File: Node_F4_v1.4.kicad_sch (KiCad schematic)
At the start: 87 parts, among them J1 Screw_Terminal_01x02, J3 Screw_Terminal_01x02, J4 Screw_Terminal_01x02, J5 Screw_Terminal_01x03, J6 Conn_01x16_Female, J7 Conn_01x08_Male, J8 STLINK, Q1 P_Mosfet, SW1 SW_Push, U10 Ai-Thinker-Ra-02, U2 PCF8574A, U3 AMS1117-3.3, U4 DS3231M, U5 MAX485E, U6 STM32F411CEUx, U7 Trans_MOSFET, U8 Trans_MOSFET, U9 W25Q128JVS, Y1 25MHz

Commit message: sua nguon
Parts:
- R19: footprint Resistor_SMD:R_0603_1608Metric -> Resistor_SMD:R_0805_2012Metric
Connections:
- net L: now also J3.2 (Pin_2), J4.2 (Pin_2)
- net N: now also RL1.2, RL2.2; no longer J3.1 (Pin_1), J4.1 (Pin_1), RL1.3, RL2.3
- removed net relay_1: J4.2 (Pin_2), RL1.2
- removed net relay_2: J3.2 (Pin_2), RL2.2
- new net N1: J4.1 (Pin_1), RL1.3
- new net N2: J3.1 (Pin_1), RL2.3
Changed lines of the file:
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@@
     (stroke (width 0) (type default) (color 0 0 0 0))
   )
-  (wire (pts (xy 360.68 38.1) (xy 365.76 38.1))
+  (wire (pts (xy 360.68 38.1) (xy 370.84 38.1))
     (stroke (width 0) (type default) (color 0 0 0 0))
   )
@@
     (effects (font (size 1.27 1.27)) (justify left bottom))
   )
-  (label "N" (at 62.23 189.23 0)
+  (label "N2" (at 62.23 189.23 0)
     (effects (font (size 1.27 1.27)) (justify left bottom))
   )
@@
     (effects (font (size 1.27 1.27)) (justify right bottom))
   )
+  (label "N" (at 367.03 68.58 180)
+    (effects (font (size 1.27 1.27)) (justify right bottom))
+  )
   (label "TFT_RS" (at 64.77 224.79 0)
     (effects (font (size 1.27 1.27)) (justify left bottom))
@@
     (effects (font (size 1.27 1.27)) (justify right bottom))
   )
-  (label "relay_2" (at 62.23 191.77 0)
-    (effects (font (size 1.27 1.27)) (justify left bottom))
-  )
   (label "TFT_CS" (at 240.03 189.23 0)
     (effects (font (size 1.27 1.27)) (justify left bottom))
@@
     (effects (font (size 1.27 1.27)) (justify left bottom))
   )
+  (label "N" (at 368.3 22.86 0)
+    (effects (font (size 1.27 1.27)) (justify left bottom))
+  )
   (label "TFT_DB7" (at 240.03 201.93 0)
     (effects (font (size 1.27 1.27)) (justify left bottom))
@@
     (effects (font (size 1.27 1.27)) (justify left bottom))
   )
-  (label "relay_1" (at 367.03 68.58 180)
-    (effects (font (size 1.27 1.27)) (justify right bottom))
-  )
-  (label "N" (at 62.23 195.58 0)
+  (label "N1" (at 62.23 195.58 0)
     (effects (font (size 1.27 1.27)) (justify left bottom))
   )
@@
     (effects (font (size 1.27 1.27)) (justify left bottom))
   )
-  (label "relay_2" (at 368.3 22.86 180)
-    (effects (font (size 1.27 1.27)) (justify right bottom))
+  (label "L" (at 62.23 198.12 0)
+    (effects (font (size 1.27 1.27)) (justify left bottom))
   )
   (label "TFT_DB2" (at 64.77 242.57 0)
@@
     (effects (font (size 1.27 1.27)) (justify left bottom))
   )
-  (label "N" (at 367.03 83.82 180)
+  (label "N1" (at 367.03 83.82 180)
     (effects (font (size 1.27 1.27)) (justify right bottom))
   )
@@
     (effects (font (size 1.27 1.27)) (justify left bottom))
   )
+  (label "L" (at 62.23 191.77 0)
+    (effects (font (size 1.27 1.27)) (justify left bottom))
+  )
   (label "P6" (at 107.95 199.39 0)
     (effects (font (size 1.27 1.27)) (justify left bottom))
@@
     (effects (font (size 1.27 1.27)) (justify right bottom))
   )
-  (label "relay_1" (at 62.23 198.12 0)
-    (effects (font (size 1.27 1.27)) (justify left bottom))
-  )
   (label "SPI_SCK" (at 340.36 201.93 0)
     (effects (font (size 1.27 1.27)) (justify left bottom))
@@
     (effects (font (size 1.27 1.27)) (justify left bottom))
   )
-  (label "N" (at 365.76 38.1 180)
+  (label "N2" (at 370.84 38.1 180)
     (effects (font (size 1.27 1.27)) (justify right bottom))
   )
@@
     (property "Reference" "R19" (id 0) (at 58.42 228.6 90))
     (property "Value" "100R" (id 1) (at 58.42 231.14 90))
-    (property "Footprint" "Resistor_SMD:R_0603_1608Metric" (id 2) (at 58.42 236.728 90)
+    (property "Footprint" "Resistor_SMD:R_0805_2012Metric" (id 2) (at 58.42 236.728 90)
       (effects (font (size 1.27 1.27)) hide)
     )
@@
     )
     (path "/80ad6425-d2d2-43d9-b7b6-efb83d17a2ad"
-      (reference "R19") (unit 1) (value "100R") (footprint "Resistor_SMD:R_0603_1608Metric")
+      (reference "R19") (unit 1) (value "100R") (footprint "Resistor_SMD:R_0805_2012Metric")
     )
     (path "/d640f459-d51e-4801-88fe-79ada9526d0a"

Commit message: thay terminal
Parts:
- removed J1, J3, J4: Screw_Terminal_01x02, TerminalBlock_Phoenix:TerminalBlock_Phoenix_MKDS-1,5-2-5.08_1x02_P5.08mm_Horizontal, symbol Connector:Screw_Terminal_01x02
- removed J5: Screw_Terminal_01x03, TerminalBlock_Phoenix:TerminalBlock_Phoenix_MKDS-1,5-3-5.08_1x03_P5.08mm_Horizontal, symbol Connector:Screw_Terminal_01x03
- added J?: Screw_Terminal_01x09, TerminalBlock_Phoenix:TerminalBlock_Phoenix_MKDS-1,5-9_1x09_P5.00mm_Horizontal, symbol Connector:Screw_Terminal_01x09
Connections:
- net A+: now also J?.7 (Pin_7)
- net B-: now also J?.9 (Pin_9)
- net GNDREF: now also J?.8 (Pin_8)
- net L: now also J?.1 (Pin_1), J?.4 (Pin_4), J?.6 (Pin_6)
- net N: now also J?.2 (Pin_2)
- net N1: now also J?.5 (Pin_5)
- net N2: now also J?.3 (Pin_3)

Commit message: teardrop
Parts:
- gave numbers to parts that had none: 1
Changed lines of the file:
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@@
   (symbol (lib_id "Connector:Screw_Terminal_01x09") (at 54.61 194.31 0) (unit 1)
     (in_bom yes) (on_board yes) (fields_autoplaced)
-    (property "Reference" "J?" (id 0) (at 57.15 193.0399 0)
+    (property "Reference" "J1" (id 0) (at 57.15 193.0399 0)
       (effects (font (size 1.27 1.27)) (justify left))
     )
@@
   (symbol (lib_id "power:GNDREF") (at 31.75 201.93 180) (unit 1)
     (in_bom yes) (on_board yes)
-    (property "Reference" "#PWR?" (id 0) (at 31.75 195.58 0)
+    (property "Reference" "#PWR0102" (id 0) (at 31.75 195.58 0)
       (effects (font (size 1.27 1.27)) hide)
     )
@@
       (reference "#PWR0101") (unit 1) (value "+5V") (footprint "")
     )
+    (path "/af3ac857-dd8e-4784-92ee-7d191ec5a304"
+      (reference "#PWR0102") (unit 1) (value "GNDREF") (footprint "")
+    )
     (path "/f840a601-70b7-488e-8299-6289e9e09ecc"
       (reference "#PWR0103") (unit 1) (value "+3.3V") (footprint "")
@@
       (reference "#PWR0158") (unit 1) (value "GND") (footprint "")
     )
-    (path "/af3ac857-dd8e-4784-92ee-7d191ec5a304"
-      (reference "#PWR?") (unit 1) (value "GNDREF") (footprint "")
-    )
     (path "/e79c523e-5bda-47a2-9098-db791a1676cd"
       (reference "BT1") (unit 1) (value "Battery_Cell") (footprint "IVS_FOOTPRINTS:BatteryHolder_CR1220")
@@
       (reference "H4") (unit 1) (value "MountingHole") (footprint "MountingHole:MountingHole_2.2mm_M2_Pad_Via")
     )
+    (path "/a20ced64-33cc-4c5f-9ebb-67e3de71ad6f"
+      (reference "J1") (unit 1) (value "Screw_Terminal_01x09") (footprint "TerminalBlock_Phoenix:TerminalBlock_Phoenix_MKDS-1,5-9_1x09_P5.00mm_Horizontal")
+    )
     (path "/5825f3f3-cb85-465a-8d89-39ae74babb06"
       (reference "J6") (unit 1) (value "Conn_01x16_Female") (footprint "Connector_PinSocket_2.54mm:PinSocket_1x16_P2.54mm_Vertical")
@@
       (reference "J8") (unit 1) (value "STLINK") (footprint "Connector_PinHeader_2.54mm:PinHeader_1x05_P2.54mm_Vertical")
     )
-    (path "/a20ced64-33cc-4c5f-9ebb-67e3de71ad6f"
-      (reference "J?") (unit 1) (value "Screw_Terminal_01x09") (footprint "TerminalBlock_Phoenix:TerminalBlock_Phoenix_MKDS-1,5-9_1x09_P5.00mm_Horizontal")
-    )
     (path "/c09e0fa3-9a7c-4b7a-ba41-09c83225f659"

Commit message: DONE
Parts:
- removed R18: 1K, Resistor_SMD:R_0603_1608Metric, symbol Device:R
- added BZ1: Buzzer, Buzzer_Beeper:PUIAudio_SMT_0825_S_4_R, symbol Device:Buzzer
- added Q2: MMBT3904L, IVS_FOOTPRINTS:SOT23-3, symbol IVS_Symbol:MMBT3904L
- R19: value 100R -> 1K; footprint Resistor_SMD:R_0805_2012Metric -> Resistor_SMD:R_0603_1608Metric
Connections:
- net +3.3V: now also J6.8 (Pin_8), Q1.3 (D), BZ1.1 (-)
- net +5V: no longer Q1.3 (D)
- net GND: now also Q1.2 (S), R17.1, Q2.2 (E)
- net BUZZER: now reaches U6.2 (PC13)
- net BUZZER: now also R19.2
- new net: Q2.1 (B), R19.1
- new net: BZ1.2 (+), Q2.3 (C)
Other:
- note added: "BUZZER"
- moved on the sheet: BT1, C1, C10, C11, C12, C2, C22, C23, C24, C25, C26, C4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

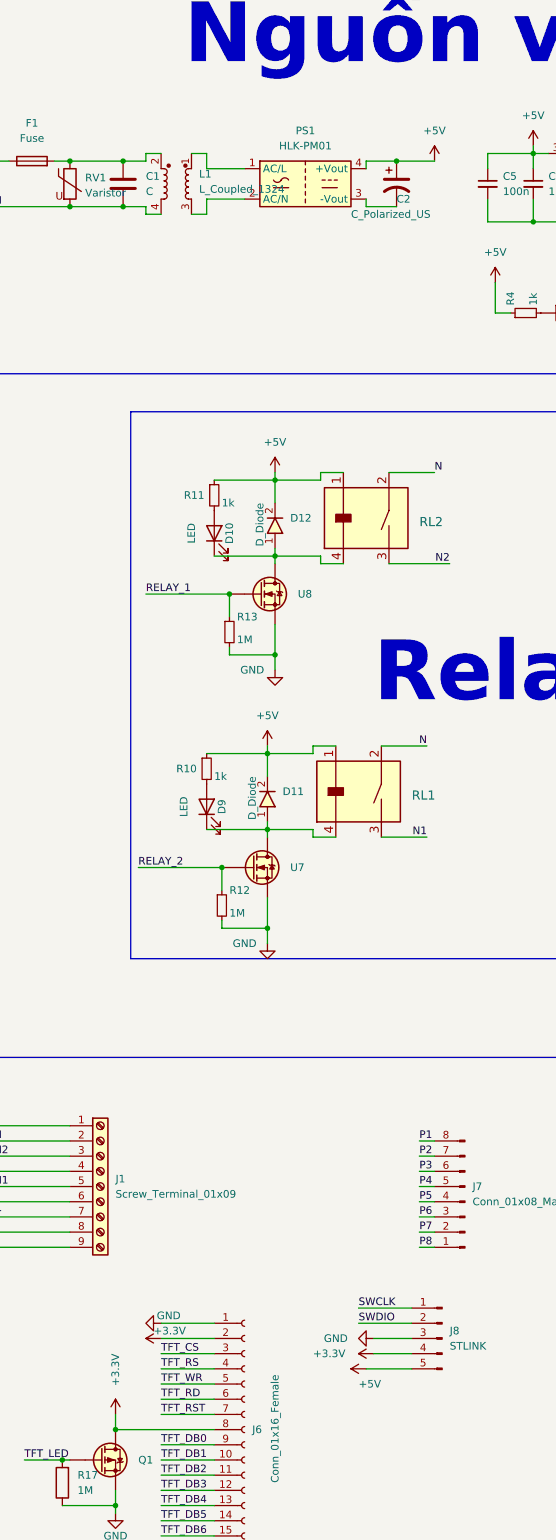
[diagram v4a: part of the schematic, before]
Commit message: Fix GND alu cap at output HLK
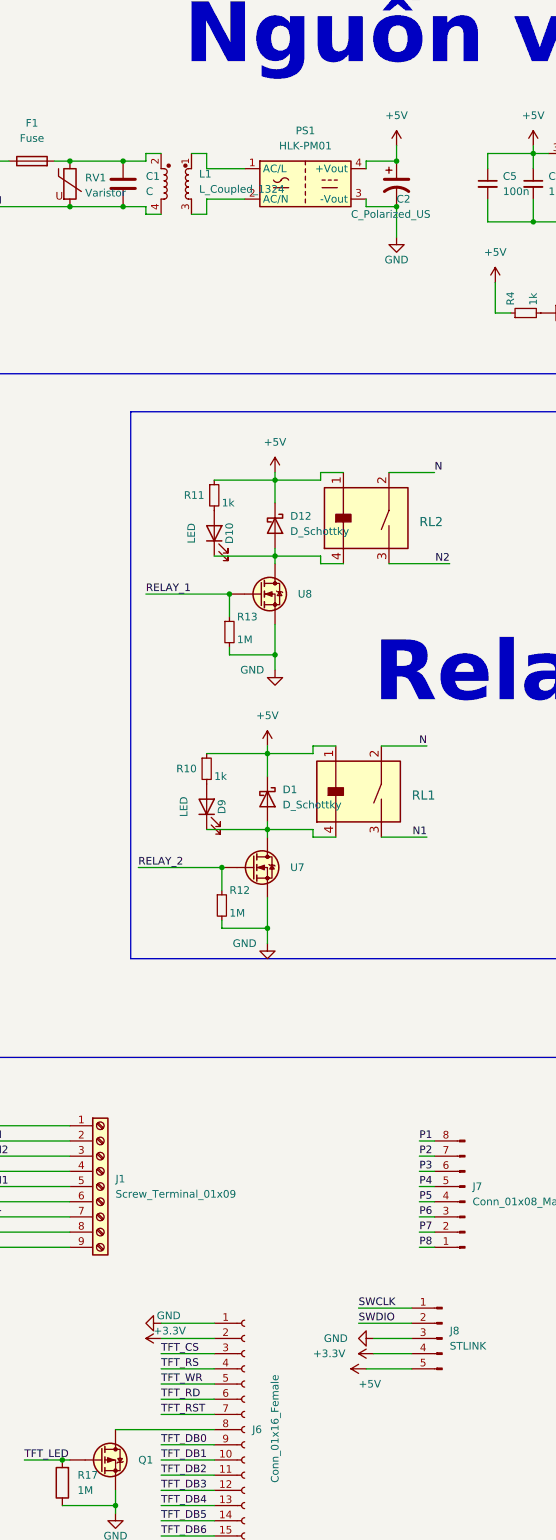
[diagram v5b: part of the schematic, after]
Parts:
- removed D11, D12: D_Diode, IVS_FOOTPRINTS:D_SOD-123F, symbol IVS_Symbol:D_Diode
- added D1, D12: D_Schottky, IVS_FOOTPRINTS:D_SOD-123F, symbol Device:D_Schottky
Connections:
- net +3.3V: no longer J6.8 (Pin_8), Q1.3 (D)
- net +5V: now also D1.1 (K), D12.1 (K)
- net GND: now also C2.2, PS1.3 (-Vout)
- net at D9.1 (K), RL1.4, U7.3 (D): now also D1.2 (A)
- net at D10.1 (K), RL2.4, U8.3 (D): now also D12.2 (A)
- new net: J6.8 (Pin_8), Q1.3 (D)
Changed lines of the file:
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@@
   (junction (at 59.69 106.68) (diameter 0) (color 0 0 0 0)
   )
+  (junction (at 114.3 106.68) (diameter 0) (color 0 0 0 0)
+  )
   (junction (at 368.3 300.99) (diameter 0) (color 0 0 0 0)
   )
@@
   (junction (at 241.3 132.08) (diameter 0) (color 0 0 0 0)
   )
+  (junction (at 114.3 99.06) (diameter 0) (color 0 0 0 0)
+  )
   (junction (at 273.05 215.9) (diameter 0) (color 0 0 0 0)
   )
@@
   (junction (at 439.42 128.27) (diameter 0) (color 0 0 0 0)
   )
-  (junction (at 67.31 311.15) (diameter 0) (color 0 0 0 0)
-  )
   (junction (at 137.16 97.79) (diameter 0) (color 0 0 0 0)
   )
@@
   (junction (at 271.78 135.89) (diameter 0) (color 0 0 0 0)
   )
-  (junction (at 114.3 99.06) (diameter 0) (color 0 0 0 0)
-  )
   (junction (at 270.51 215.9) (diameter 0) (color 0 0 0 0)
   )
@@
     (stroke (width 0) (type default) (color 0 0 0 0))
   )
+  (wire (pts (xy 114.3 96.52) (xy 114.3 99.06))
+    (stroke (width 0) (type default) (color 0 0 0 0))
+  )
   (wire (pts (xy 110.49 295.91) (xy 116.84 295.91))
     (stroke (width 0) (type default) (color 0 0 0 0))
@@
     (stroke (width 0) (type default) (color 0 0 0 0))
   )
-  (wire (pts (xy 67.31 308.61) (xy 67.31 311.15))
-    (stroke (width 0) (type default) (color 0 0 0 0))
-  )
   (wire (pts (xy 245.11 158.75) (xy 252.73 158.75))
     (stroke (width 0) (type default) (color 0 0 0 0))
@@
     (stroke (width 0) (type default) (color 0 0 0 0))
   )
+  (wire (pts (xy 114.3 106.68) (xy 114.3 111.76))
+    (stroke (width 0) (type default) (color 0 0 0 0))
+  )
   (wire (pts (xy 93.98 181.61) (xy 93.98 184.15))
     (stroke (width 0) (type default) (color 0 0 0 0))
@@
     (stroke (width 0) (type default) (color 0 0 0 0))
   )
-  (wire (pts (xy 114.3 99.06) (xy 120.65 99.06))
-    (stroke (width 0) (type default) (color 0 0 0 0))
-  )
   (wire (pts (xy 271.78 85.09) (xy 271.78 86.36))
     (stroke (width 0) (type default) (color 0 0 0 0))
@@
     (effects (font (size 1.27 1.27)) (justify left bottom))
   )
-  (symbol (lib_id "IVS_Symbol:D_Diode") (at 92.71 204.47 270) (unit 1)
-    (in_bom yes) (on_board yes)
-    (property "Reference" "D11" (id 0) (at 95.25 204.4699 90)
-      (effects (font (size 1.27 1.27)) (justify left))
-    )
-    (property "Value" "D_Diode" (id 1) (at 90.17 201.93 0)
-      (effects (font (size 1.27 1.27)) (justify left))
-    )
-    (property "Footprint" "IVS_FOOTPRINTS:D_SOD-123F" (id 2) (at 92.71 204.47 0)
-      (effects (font (size 1.27 1.27)) hide)
-    )
-    (property "Datasheet" "" (id 3) (at 92.71 204.47 0)
-      (effects (font (size 1.27 1.27)) hide)
-    )
-    (pin "1")
-    (pin "2")
-  )
   (symbol (lib_id "Switch:SW_Push") (at 228.6 147.32 90) (unit 1)
     (in_bom yes) (on_board yes)
@@
     (pin "1")
   )
+  (symbol (lib_id "Device:D_Schottky") (at 93.98 160.02 270) (unit 1)
+    (in_bom yes) (on_board yes) (fields_autoplaced)
+    (property "Reference" "D12" (id 0) (at 96.52 158.4324 90)
+      (effects (font (size 1.27 1.27)) (justify left))
+    )
+    (property "Value" "D_Schottky" (id 1) (at 96.52 160.9724 90)
+      (effects (font (size 1.27 1.27)) (justify left))
+    )
+    (property "Footprint" "IVS_FOOTPRINTS:D_SOD-123F" (id 2) (at 93.98 160.02 0)
+      (effects (font (size 1.27 1.27)) hide)
+    )
+    (property "Datasheet" "~" (id 3) (at 93.98 160.02 0)
+      (effects (font (size 1.27 1.27)) hide)
+    )
+    (pin "1")
+    (pin "2")
+  )
   (symbol (lib_id "Timer_RTC:DS3231M") (at 450.85 146.05 0) (unit 1)
     (in_bom yes) (on_board yes) (fields_autoplaced)
@@
     (pin "2")
   )
-  (symbol (lib_id "IVS_Symbol:D_Diode") (at 93.98 158.75 270) (unit 1)
-    (in_bom yes) (on_board yes)
-    (property "Reference" "D12" (id 0) (at 96.52 158.7499 90)
-      (effects (font (size 1.27 1.27)) (justify left))
-    )
-    (property "Value" "D_Diode" (id 1) (at 91.44 156.21 0)
-      (effects (font (size 1.27 1.27)) (justify left))
-    )
-    (property "Footprint" "IVS_FOOTPRINTS:D_SOD-123F" (id 2) (at 93.98 158.75 0)
-      (effects (font (size 1.27 1.27)) hide)
-    )
-    (property "Datasheet" "" (id 3) (at 93.98 158.75 0)
-      (effects (font (size 1.27 1.27)) hide)
-    )
-    (pin "1")
-    (pin "2")
-  )
   (symbol (lib_id "power:GND") (at 233.68 59.69 270) (unit 1)
     (in_bom yes) (on_board yes)
@@
     (pin "3")
   )
+  (symbol (lib_id "Device:D_Schottky") (at 92.71 205.74 270) (unit 1)
+    (in_bom yes) (on_board yes) (fields_autoplaced)
+    (property "Reference" "D1" (id 0) (at 95.25 204.1524 90)
+      (effects (font (size 1.27 1.27)) (justify left))
+    )
+    (property "Value" "D_Schottky" (id 1) (at 95.25 206.6924 90)
+      (effects (font (size 1.27 1.27)) (justify left))
+    )
+    (property "Footprint" "IVS_FOOTPRINTS:D_SOD-123F" (id 2) (at 92.71 205.74 0)
+      (effects (font (size 1.27 1.27)) hide)
+    )
+    (property "Datasheet" "~" (id 3) (at 92.71 205.74 0)
+      (effects (font (size 1.27 1.27)) hide)
+    )
+    (pin "1")
+    (pin "2")
+  )
   (symbol (lib_id "power:+3.3V") (at 74.93 295.91 90) (unit 1)
     (in_bom yes) (on_board yes)
@@
     (pin "2")
   )
-  (symbol (lib_id "power:+5V") (at 120.65 99.06 0) (unit 1)
+  (symbol (lib_id "power:+5V") (at 114.3 96.52 0) (unit 1)
     (in_bom yes) (on_board yes) (fields_autoplaced)
-    (property "Reference" "#PWR0101" (id 0) (at 120.65 102.87 0)
-      (effects (font (size 1.27 1.27)) hide)
-    )
-    (property "Value" "+5V" (id 1) (at 120.65 93.98 0))
-    (property "Footprint" "" (id 2) (at 120.65 99.06 0)
+    (property "Reference" "#PWR0101" (id 0) (at 114.3 100.33 0)
       (effects (font (size 1.27 1.27)) hide)
     )
-    (property "Datasheet" "" (id 3) (at 120.65 99.06 0)
+    (property "Value" "+5V" (id 1) (at 114.3 91.44 0))
+    (property "Footprint" "" (id 2) (at 114.3 96.52 0)
       (effects (font (size 1.27 1.27)) hide)
     )
-    (pin "1")
-  )
-  (symbol (lib_id "power:+3.3V") (at 67.31 308.61 0) (unit 1)
-    (in_bom yes) (on_board yes)
-    (property "Reference" "#PWR0104" (id 0) (at 67.31 312.42 0)
-      (effects (font (size 1.27 1.27)) hide)
-    )
-    (property "Value" "+3.3V" (id 1) (at 67.31 298.45 90)
-      (effects (font (size 1.27 1.27)) (justify right))
-    )
-    (property "Footprint" "" (id 2) (at 67.31 308.61 0)
-      (effects (font (size 1.27 1.27)) hide)
-    )
-    (property "Datasheet" "" (id 3) (at 67.31 308.61 0)
+    (property "Datasheet" "" (id 3) (at 114.3 96.52 0)
       (effects (font (size 1.27 1.27)) hide)
     )
@@
     (pin "1")
   )
+  (symbol (lib_id "power:GND") (at 114.3 111.76 0) (unit 1)
+    (in_bom yes) (on_board yes)
+    (property "Reference" "#PWR0104" (id 0) (at 114.3 118.11 0)
+      (effects (font (size 1.27 1.27)) hide)
+    )
+    (property "Value" "GND" (id 1) (at 114.3 115.57 0))
+    (property "Footprint" "" (id 2) (at 114.3 111.76 0)
+      (effects (font (size 1.27 1.27)) hide)
+    )
+    (property "Datasheet" "" (id 3) (at 114.3 111.76 0)
+      (effects (font (size 1.27 1.27)) hide)
+    )
+    (pin "1")
+  )
   (symbol (lib_id "power:+3.3V") (at 388.62 276.86 270) (unit 1)
     (in_bom yes) (on_board yes) (fields_autoplaced)
@@
       (reference "#PWR0103") (unit 1) (value "+3.3V") (footprint "")
     )
-    (path "/aac6ce4f-65e1-4a56-81bf-9efefc48b274"
-      (reference "#PWR0104") (unit 1) (value "+3.3V") (footprint "")
+    (path "/b16ecafa-8934-4c18-b391-f71f264c8900"
+      (reference "#PWR0104") (unit 1) (value "GND") (footprint "")
     )
     (path "/50e1803d-3f59-4f8f-b9ab-d1e6f1040027"
@@
       (reference "C26") (unit 1) (value "0.1u") (footprint "Capacitor_SMD:C_0603_1608Metric")
     )
+    (path "/92c9b5d5-542d-4fce-83d8-15fad092b3f3"
+      (reference "D1") (unit 1) (value "D_Schottky") (footprint "IVS_FOOTPRINTS:D_SOD-123F")
+    )
     (path "/acd540d9-9b51-40e6-ab91-200738b1dd12"
       (reference "D3") (unit 1) (value "LED") (footprint "LED_SMD:LED_0603_1608Metric")
@@
       (reference "D10") (unit 1) (value "LED") (footprint "LED_SMD:LED_0603_1608Metric")
     )
-    (path "/0099199c-66ee-48f9-826c-0e08394d99e5"
-      (reference "D11") (unit 1) (value "D_Diode") (footprint "IVS_FOOTPRINTS:D_SOD-123F")
-    )
-    (path "/6e01c1c1-0611-499b-bcc8-6de62c25a2c3"
-      (reference "D12") (unit 1) (value "D_Diode") (footprint "IVS_FOOTPRINTS:D_SOD-123F")
+    (path "/0804e302-ba94-471f-9b92-96ab4d74146c"
+      (reference "D12") (unit 1) (value "D_Schottky") (footprint "IVS_FOOTPRINTS:D_SOD-123F")
     )
     (path "/f590fa38-a9ae-4094-ab10-ae9ef3fa05ac"
